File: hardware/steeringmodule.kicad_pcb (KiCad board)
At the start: 2 copper layers, 144 x 59.5 mm, 88 parts, among them J101 Conn_01x02, J102 PotConnector, J103 Conn_01x02, U201 MCP2561-E/SN, U202 MCP2515-I/SO, U301 LM7805_TO220, U401 ATMEGA328P-PU, U601 BTS7960B, U602 BTS7960B, U701 INA826_D_8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

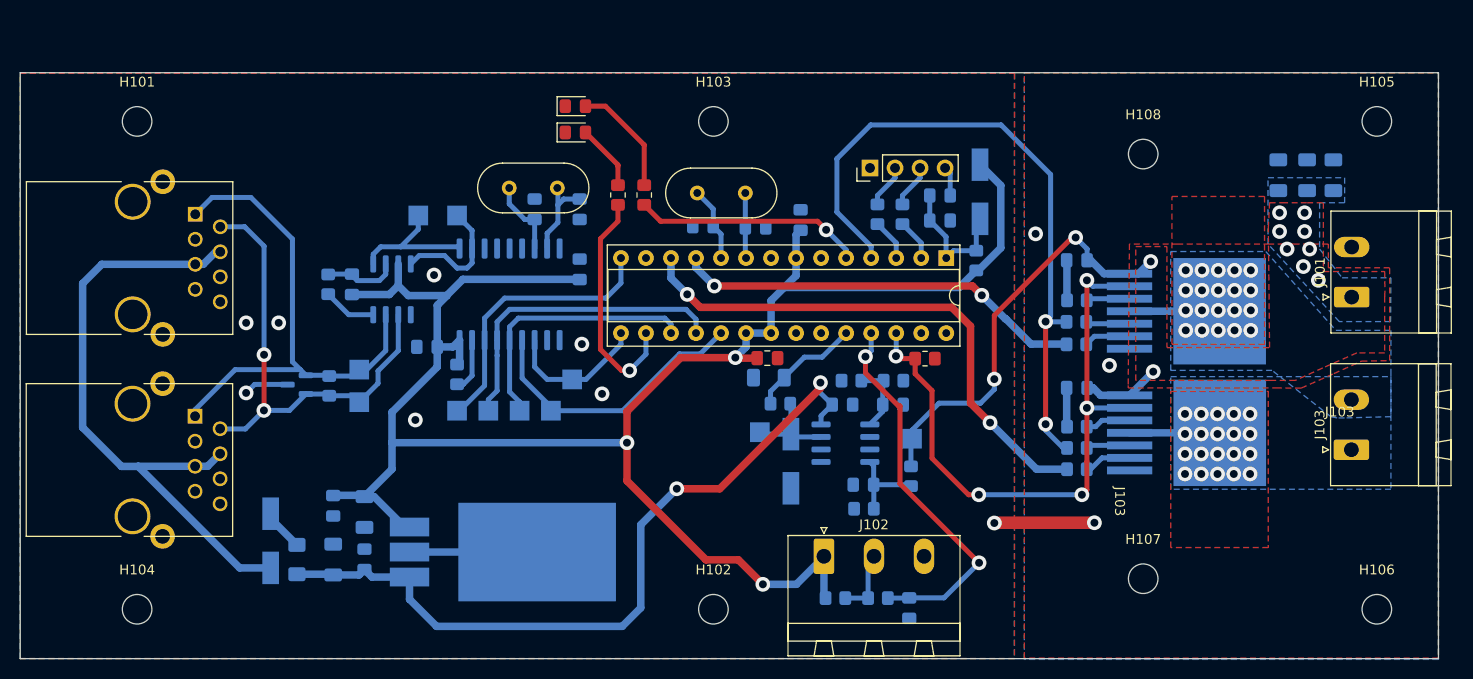
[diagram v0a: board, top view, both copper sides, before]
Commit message: hardware: K78L15 to supply INA826 and other changes
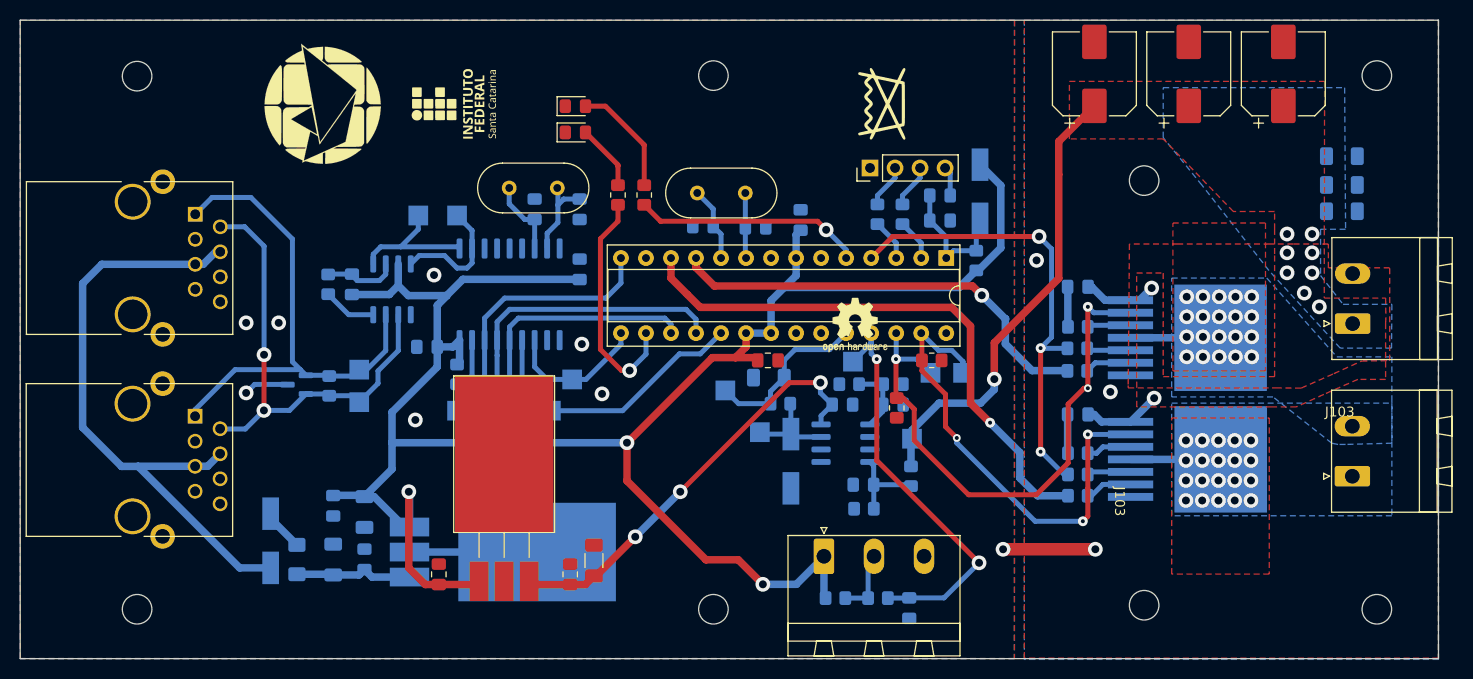
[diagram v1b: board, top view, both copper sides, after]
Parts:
- added C305: 100nF, Capacitor_SMD:C_0805_2012Metric_Pad1.18x1.45mm_HandSolder, F.Cu at (101.7, 114.6)
- added C306: 100nF, Capacitor_SMD:C_0805_2012Metric_Pad1.18x1.45mm_HandSolder, F.Cu at (115.1, 114.6)
- added C307: 1uF, Capacitor_SMD:C_1206_3216Metric_Pad1.33x1.80mm_HandSolder, F.Cu at (117.5, 113.2)
- added C604: C_Polarized_Small, Capacitor_SMD:CP_Elec_8x10, F.Cu at (187.5, 63.8)
- added C605: C_Polarized_Small, Capacitor_SMD:CP_Elec_8x10, F.Cu at (177.9, 63.8)
- added C606: C_Polarized_Small, Capacitor_SMD:CP_Elec_8x10, F.Cu at (168.3, 63.8)
- added LOGO101: Logo_Open_Hardware_Small, Symbol:OSHW-Logo2_7.3x6mm_SilkScreen, F.Cu at (144.0, 89.2)
- added RIS601: 1k, Resistor_SMD:R_0805_2012Metric_Pad1.20x1.40mm_HandSolder, F.Cu at (151.8, 92.8)
- added SYM101: SYM_Flash_Small, KicadZeniteSolarLibrary18:symbol_logoZenite, B.Cu at (89.8, 67.2)
- added SYM102: SYM_Flash_Small, KicadZeniteSolarLibrary18:symbol_logoZenite, F.Cu at (89.9, 66.8)
- added SYM103: SYM_Flash_Small, KicadZeniteSolarLibrary18:synbol_logoifsc, F.Cu at (103.3, 66.8)
- added SYM104: SYM_Flash_Small, KicadZeniteSolarLibrary18:synbol_logoifsc, B.Cu at (103.3, 66.7)
- added SYM105: SYM_Radioactive_Radiation_Small, KicadZeniteSolarLibrary18:symbol_naolavar, F.Cu at (146.7, 66.8)
- added TP501: VBAT, TestPoint:TestPoint_Pad_2.0x2.0mm, B.Cu at (130.8, 95.9)
- added TP502: POT, TestPoint:TestPoint_Pad_2.0x2.0mm, B.Cu at (143.8, 93.0)
- added TP503: IS1, TestPoint:TestPoint_Pad_2.0x2.0mm, B.Cu at (151.6, 94.1)
- added TP504: IS2, TestPoint:TestPoint_Pad_2.0x2.0mm, B.Cu at (154.9, 94.1)
- added U302: K78L15-1000R3, KicadZeniteSolarLibrary18:TO-220-3_Horizontal_TabDown_SMD, F.Cu at (105.8, 114.0)
- moved C601 6.73 mm to (193.4, 72.1), turned to 0 degrees
- moved RIS1 5.77 mm to (148.2, 97.7), turned to -90 degrees
- moved H103 4.65 mm to (129.6, 63.9)
- moved H105 4.65 mm to (196.9, 63.9)
- moved H101 4.59 mm to (71.1, 64.0)
- moved C603 3.76 mm to (193.4, 77.7), turned to 0 degrees
- moved C602 3.67 mm to (193.4, 75.0), turned to 0 degrees
- moved U602 2.69 mm to (177.7, 102.9)
- moved H107 2.69 mm to (173.3, 117.7)
- moved H108 2.69 mm to (173.3, 74.6)
- moved J101 2.69 mm to (194.5, 89.1)
- moved J103 2.69 mm to (194.5, 104.6)
- moved RINH1 2.69 mm to (166.5, 91.6)
- moved RSR1 2.69 mm to (166.6, 89.4)
- moved RSR2 2.69 mm to (166.6, 102.3)
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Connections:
- C301 pad 1: /+18V -> /POWER SUPPLY/+18V_OUT
- C302 pad 1: /+18V -> /POWER SUPPLY/+18V_OUT
- C704 pad 1: /+18V -> /+15V
- F301 pad 2: /+18V -> /POWER SUPPLY/+18V_OUT
- RIS1 pad 1: /HBRIDGE/IS -> /HBRIDGE/IS1
- U301 pad 1: /+18V -> /POWER SUPPLY/+18V_OUT
- U401 pad 26: /HBRIDGE/IS -> /HBRIDGE/IS1
- U401 pad 27: unconnected-(U401-Pad27) -> /HBRIDGE/IS2
- U601 pad 6: /HBRIDGE/IS -> /HBRIDGE/IS1
- U602 pad 6: /HBRIDGE/IS -> /HBRIDGE/IS2
- U701 pad 8: /+18V -> /+15V
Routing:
- net /+18V: track 77.7 -> 0.00 mm, vias 2 -> 0
- net /HBRIDGE/IS: track 62.9 -> 0.00 mm, vias 5 -> 0
- net /HBRIDGE/IS1: track 0.00 -> 56.9 mm, vias 0 -> 3
- net /HBRIDGE/IS2: track 0.00 -> 48.7 mm, vias 0 -> 3
- net /+15V: track 0.00 -> 43.4 mm, vias 0 -> 3
- net /HBRIDGE/INH: track 67.9 -> 47.3 mm, vias 2 -> 3
- net +5V: track 191.4 -> 209.0 mm
- net /POWER SUPPLY/+18V_OUT: track 0.00 -> 11.9 mm
- net /HBRIDGE/VS1: track 51.2 -> 62.3 mm, vias 12 -> 11
- net /MCU/VBAT: track 11.4 -> 17.6 mm
- net /MCU/POTVAL: track 39.0 -> 42.1 mm
- net /HBRIDGE/INPUT1: track 41.8 -> 44.6 mm, vias 2 -> 1
- net /HBRIDGE/INPUT2: track 54.9 -> 57.6 mm, vias 2 -> 1
- net GND: track 43.0 -> 42.2 mm
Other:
- board size 144 x 59.5 mm -> 144 x 64.8 mm

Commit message: hardware: silkscreen updated with JLC. Finished.
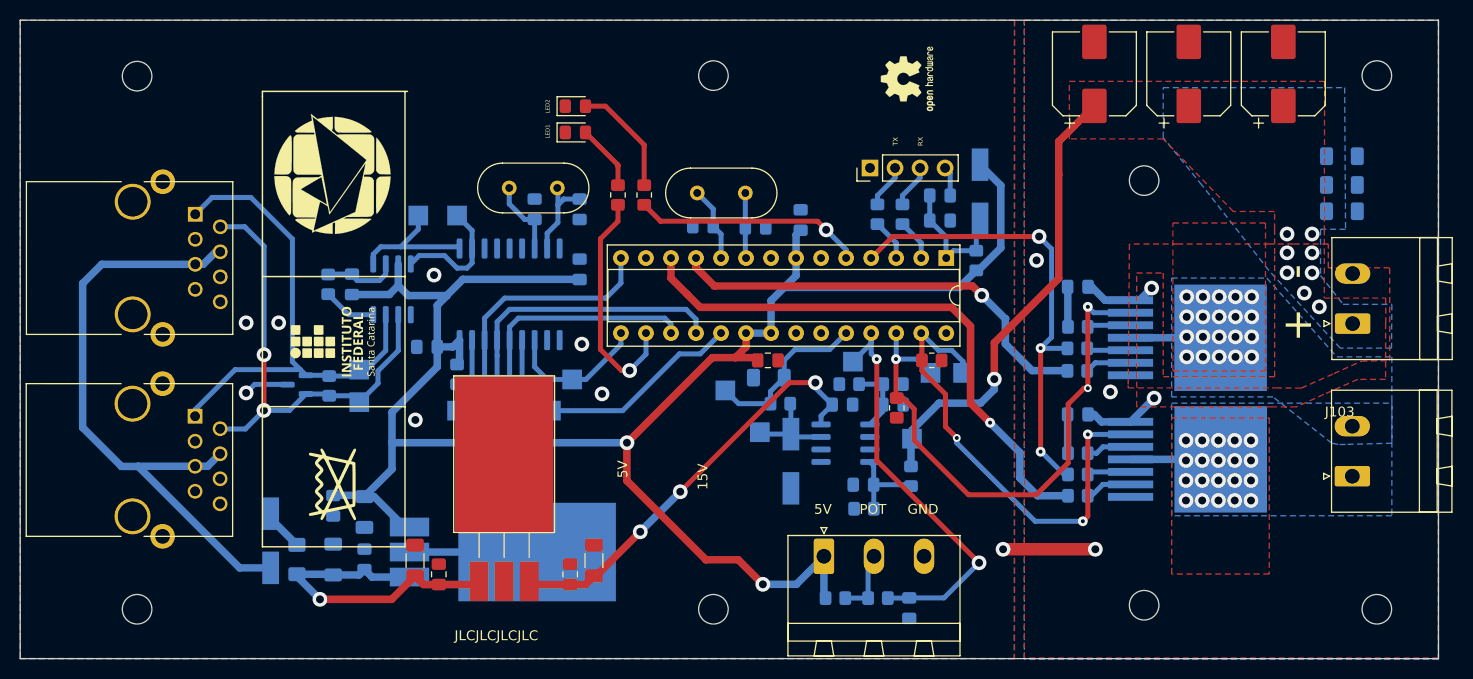
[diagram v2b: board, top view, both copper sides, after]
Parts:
- added C308: 1uF, Capacitor_SMD:C_1206_3216Metric_Pad1.33x1.80mm_HandSolder, F.Cu at (99.3, 113.2)
- moved SYM105 67.8 mm to (90.9, 105.4)
- moved SYM103 27.1 mm to (90.9, 90.9)
- moved LOGO101 25.6 mm to (149.4, 64.3), turned to 90 degrees
- moved SYM102 7.18 mm to (90.9, 73.9)
- moved SYM101 2.16 mm to (91.9, 67.1)
- moved SYM104 1.40 mm to (104.6, 66.8)
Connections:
- C301 pad 1: /POWER SUPPLY/+18V_OUT -> /POWER SUPPLY/18V
- C302 pad 1: /POWER SUPPLY/+18V_OUT -> /POWER SUPPLY/18V
- C305 pad 1: +5V -> /POWER SUPPLY/18V
- F301 pad 2: /POWER SUPPLY/+18V_OUT -> /POWER SUPPLY/18V
- U301 pad 1: /POWER SUPPLY/+18V_OUT -> /POWER SUPPLY/18V
- U302 pad 1: +5V -> /POWER SUPPLY/18V
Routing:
- net /POWER SUPPLY/18V: track 0.00 -> 33.1 mm, vias 0 -> 1
- net +5V: track 209.0 -> 189.7 mm, vias 3 -> 2
- net /POWER SUPPLY/+18V_OUT: track 11.9 -> 0.00 mm
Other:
- board text added: "+"
- board text added: "-"
- board text added: "15V"
- board text added: "5V"
- board text added: "CAN_H"
- board text added: "CAN_L"
- board text added: "GND"
- board text added: "INT"
- board text added: "IS1"
- board text added: "IS2"
- board text added: "JLCJLCJLCJLC"
- board text added: "LED1"
- board text added: "LED2"
- board text added: "POT"
- board text added: "RX"
- board text added: "RXCAN"
- board text added: "SCK"
- board text added: "SI"
- board text added: "SO"
- board text added: "SS"
- board text added: "TX"
- board text added: "TXCAN"
- board text added: "VBAT"
- board text added: "vbat"
